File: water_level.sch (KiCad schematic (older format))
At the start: 16 parts

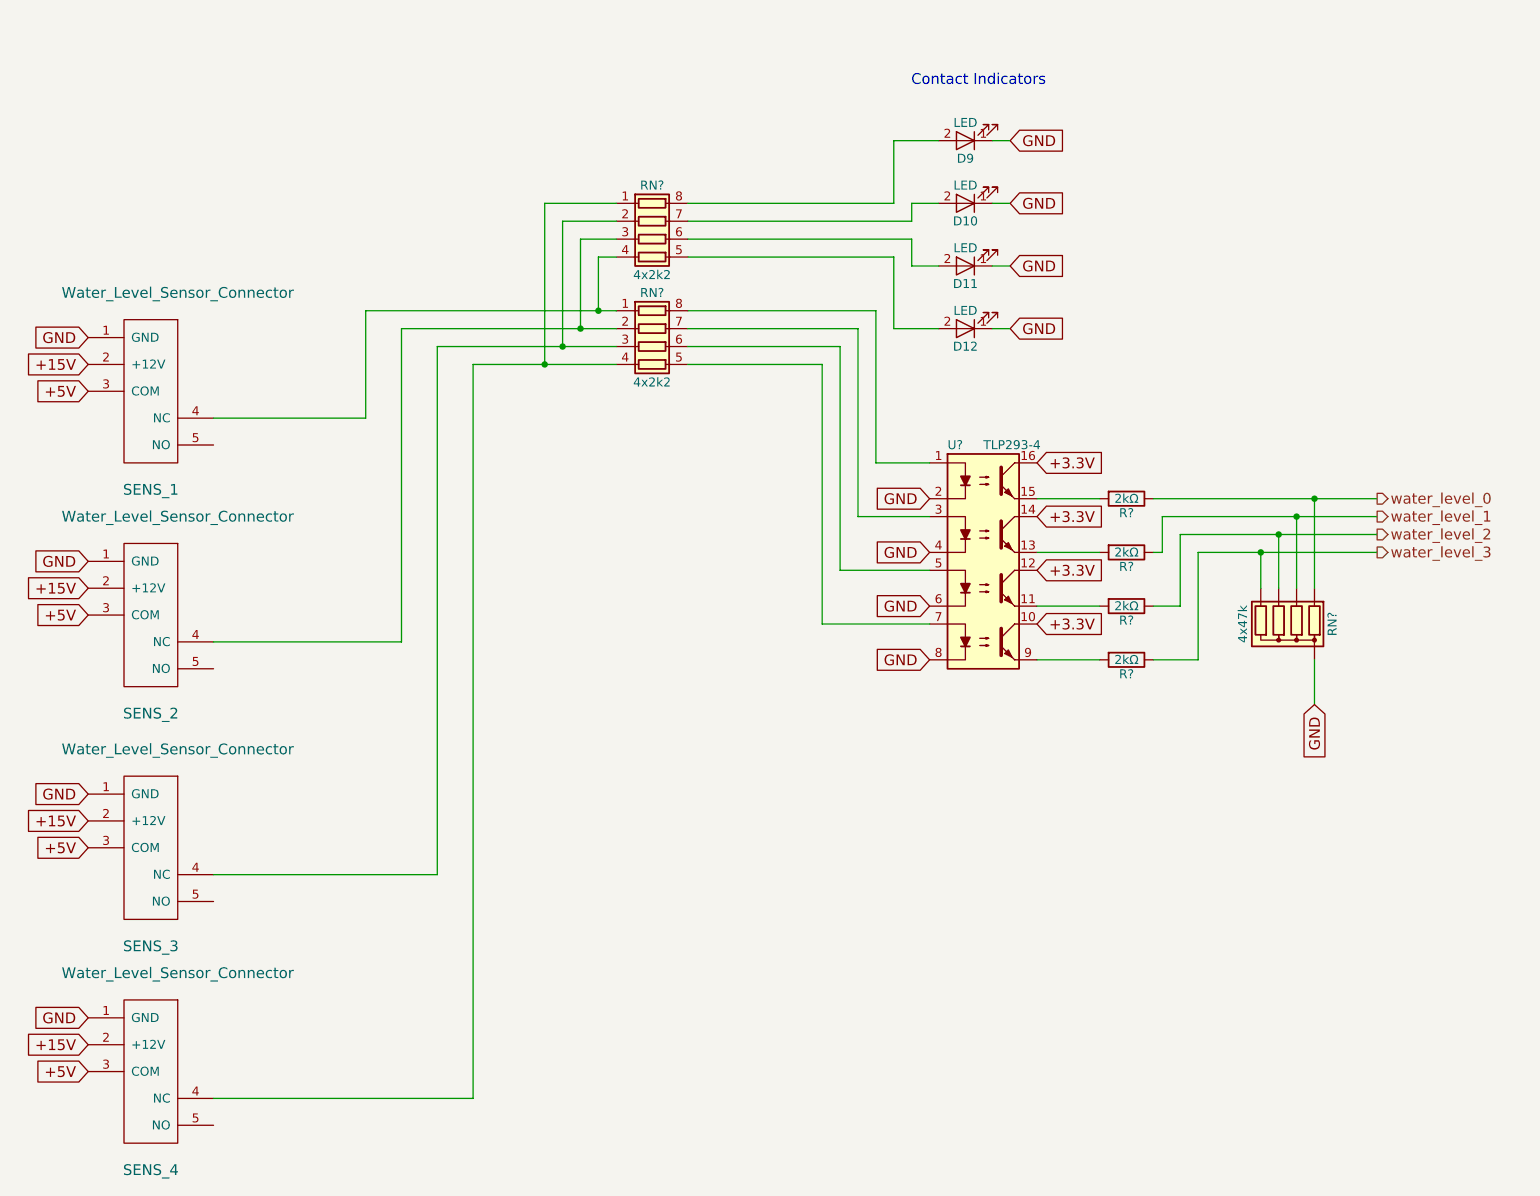
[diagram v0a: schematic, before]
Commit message: some issues fixed by the bugfixer; formal verification needed
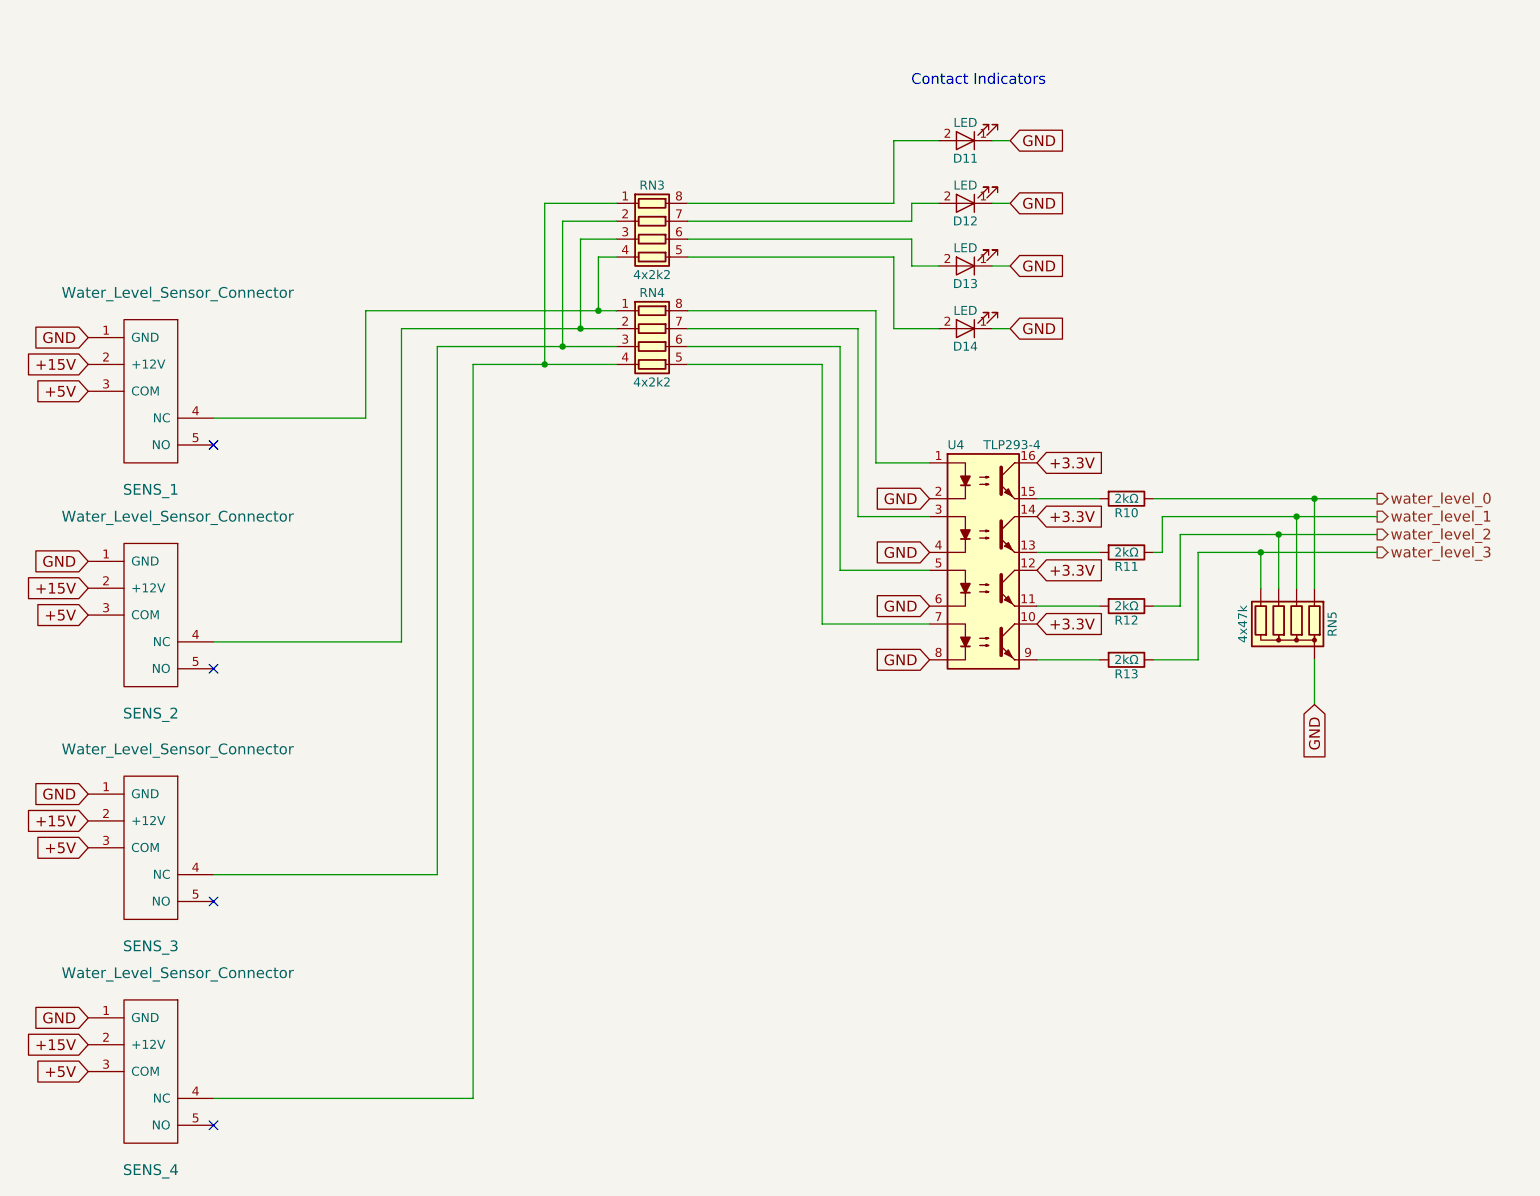
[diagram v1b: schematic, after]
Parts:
- gave numbers to parts that had none: 8
- renumbered D9 to D11, D10 to D12, D11 to D13, D12 to D14
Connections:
- no-connect marks 0 -> 4
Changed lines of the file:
@@
 $EndComp
 $Comp
-L LED D11
+L LED D13
 U 1 1 59403F87
 P 8000 2450
-F 0 "D11" H 8000 2550 50  0000 C CNN
+F 0 "D13" H 8000 2550 50  0000 C CNN
 F 1 "LED" H 8000 2350 50  0000 C CNN
 F 2 "LEDs:LED_1206" H 8000 2450 50  0001 C CNN
@@
 	8250 2450 8150 2450
 $Comp
-L LED D12
+L LED D14
 U 1 1 5940539F
 P 8000 2800
-F 0 "D12" H 8000 2900 50  0000 C CNN
+F 0 "D14" H 8000 2900 50  0000 C CNN
 F 1 "LED" H 8000 2700 50  0000 C CNN
 F 2 "LEDs:LED_1206" H 8000 2800 50  0001 C CNN
@@
 	8250 2800 8150 2800
 $Comp
-L LED D10
+L LED D12
 U 1 1 59405535
 P 8000 2100
-F 0 "D10" H 8000 2200 50  0000 C CNN
+F 0 "D12" H 8000 2200 50  0000 C CNN
 F 1 "LED" H 8000 2000 50  0000 C CNN
 F 2 "LEDs:LED_1206" H 8000 2100 50  0001 C CNN
@@
 	8250 2100 8150 2100
 $Comp
-L LED D9
+L LED D11
 U 1 1 59405613
 P 8000 1750
-F 0 "D9" H 8000 1850 50  0000 C CNN
+F 0 "D11" H 8000 1850 50  0000 C CNN
 F 1 "LED" H 8000 1650 50  0000 C CNN
 F 2 "LEDs:LED_1206" H 8000 1750 50  0001 C CNN
@@
 +5V
 $Comp
-L R_Network04 RN?
+L R_Network04 RN5
 U 1 1 59A52B59
 P 9750 4450
-F 0 "RN?" V 9450 4450 50  0000 C CNN
+F 0 "RN5" V 9450 4450 50  0000 C CNN
 F 1 "4x47k" V 9950 4450 50  0000 C CNN
 F 2 "kilibs:YC164-Yageo-Handsoldering" V 10025 4450 50  0001 C CNN
@@
 Connection ~ 9950 3750
 $Comp
-L LTV-847 U?
+L LTV-847 U4
 U 1 1 59A57625
 P 8100 4150
-F 0 "U?" H 7900 4850 50  0000 L CNN
+F 0 "U4" H 7900 4850 50  0000 L CNN
 F 1 "TLP293-4" H 8100 4850 50  0000 L CNN
 F 2 "Housings_SOIC:SOIC-16_3.9x9.9mm_Pitch1.27mm" H 7900 3550 50  0001 L CIN
@@
 $EndComp
 $Comp
-L R R?
+L R R10
 U 1 1 59A580D3
 P 8900 3750
-F 0 "R?" V 8980 3750 50  0000 C CNN
+F 0 "R10" V 8980 3750 50  0000 C CNN
 F 1 "2kΩ" V 8900 3750 50  0000 C CNN
 F 2 "Resistors_SMD:R_0603_HandSoldering" V 8830 3750 50  0001 C CNN
@@
 	5650 2100 6050 2100
 $Comp
-L R_Pack04 RN?
+L R_Pack04 RN3
 U 1 1 59A818FC
 P 6250 2300
-F 0 "RN?" V 5950 2300 50  0000 C CNN
+F 0 "RN3" V 5950 2300 50  0000 C CNN
 F 1 "4x2k2" V 6450 2300 50  0000 C CNN
 F 2 "kilibs:YC164-Yageo-Handsoldering" V 6525 2300 50  0001 C CNN
@@
 $EndComp
 $Comp
-L R_Pack04 RN?
+L R_Pack04 RN4
 U 1 1 59A81B85
 P 6250 2900
-F 0 "RN?" V 5950 2900 50  0000 C CNN
+F 0 "RN4" V 5950 2900 50  0000 C CNN
 F 1 "4x2k2" V 6450 2900 50  0000 C CNN
 F 2 "kilibs:YC164-Yageo-Handsoldering" V 6525 2900 50  0001 C CNN
@@
 $EndComp
 $Comp
-L R R?
+L R R11
 U 1 1 59A9482F
 P 8900 4050
-F 0 "R?" V 8980 4050 50  0000 C CNN
+F 0 "R11" V 8980 4050 50  0000 C CNN
 F 1 "2kΩ" V 8900 4050 50  0000 C CNN
 F 2 "Resistors_SMD:R_0603_HandSoldering" V 8830 4050 50  0001 C CNN
@@
 $EndComp
 $Comp
-L R R?
+L R R12
 U 1 1 59A94875
 P 8900 4350
-F 0 "R?" V 8980 4350 50  0000 C CNN
+F 0 "R12" V 8980 4350 50  0000 C CNN
 F 1 "2kΩ" V 8900 4350 50  0000 C CNN
 F 2 "Resistors_SMD:R_0603_HandSoldering" V 8830 4350 50  0001 C CNN
@@
 $EndComp
 $Comp
-L R R?
+L R R13
 U 1 1 59A948BA
 P 8900 4650
-F 0 "R?" V 8980 4650 50  0000 C CNN
+F 0 "R13" V 8980 4650 50  0000 C CNN
 F 1 "2kΩ" V 8900 4650 50  0000 C CNN
 F 2 "Resistors_SMD:R_0603_HandSoldering" V 8830 4650 50  0001 C CNN
@@
 	0    1    1    0
 $EndComp
+NoConn ~ 3800 4700
+NoConn ~ 3800 3450
+NoConn ~ 3800 6000
+NoConn ~ 3800 7250
 $EndSCHEMATC

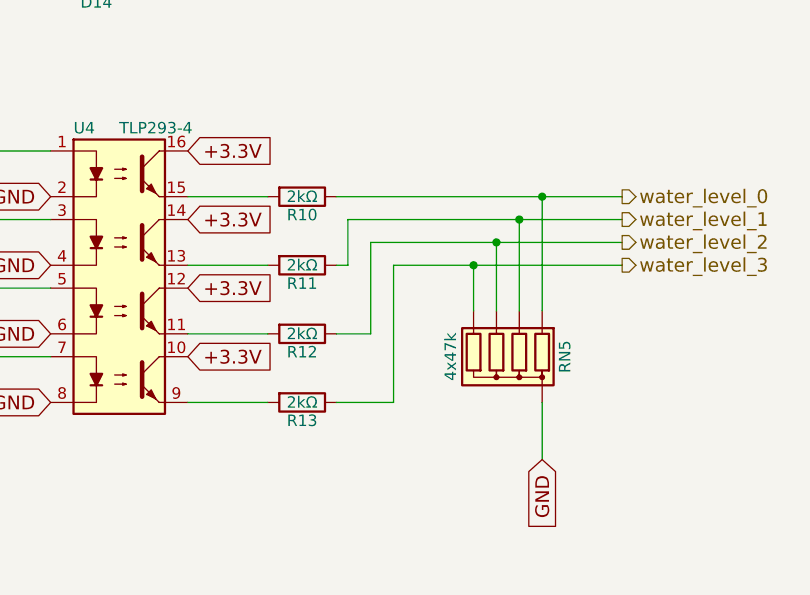
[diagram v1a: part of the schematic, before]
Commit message: I have verified the schematic a second time (except the so-dimm), and I have selected all of the components with links and footprint. I need to verify the schematic a third time and root
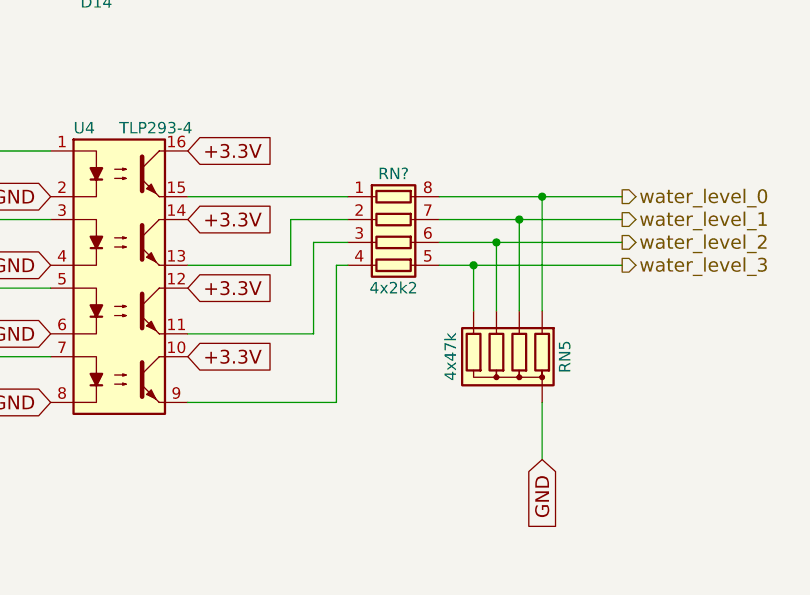
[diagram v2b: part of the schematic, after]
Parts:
- removed R10, R11, R12, R13: 2kΩ, Resistors_SMD:R_0603_HandSoldering, symbol R
- added RN?: 4x2k2, kilibs:YC164-Yageo-Handsoldering, symbol R_Pack04
- RN5: footprint kilibs:YC164-Yageo-Handsoldering -> water:YC158-Yageo-Handsoldering
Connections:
- net water_level_0: now also RN?.8 (R1.2)
- net water_level_1: now also RN?.7 (R2.2)
- net water_level_2: now also RN?.6 (R3.2)
- net water_level_3: now also RN?.5 (R4.2)
- net at U4.11: now also RN?.3 (R3.1)
- net at U4.13: now also RN?.2 (R2.1)
- net at U4.15: now also RN?.1 (R1.1)
- net at U4.9: now also RN?.4 (R4.1)
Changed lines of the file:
@@
 F 0 "RN5" V 9450 4450 50  0000 C CNN
 F 1 "4x47k" V 9950 4450 50  0000 C CNN
-F 2 "kilibs:YC164-Yageo-Handsoldering" V 10025 4450 50  0001 C CNN
+F 2 "water:YC158-Yageo-Handsoldering" V 10025 4450 50  0001 C CNN
 F 3 "http://hu.farnell.com/yageo-phycomp/yc158tjr-0747kl/resistor-network-rna310-1206-47k/dp/9236279" H 9750 4450 50  0001 C CNN
 	1    9750 4450
@@
 Wire Wire Line
 	9950 4900 9950 4650
-Wire Wire Line
-	9050 3750 10300 3750
-Wire Wire Line
-	9100 3850 10300 3850
-Wire Wire Line
-	9200 3950 10300 3950
-Wire Wire Line
-	9300 4050 10300 4050
 Wire Wire Line
 	9650 4250 9650 4050
@@
 	1    0    0    -1
 $EndComp
-$Comp
-L R R10
-U 1 1 59A580D3
-P 8900 3750
-F 0 "R10" V 8980 3750 50  0000 C CNN
-F 1 "2kΩ" V 8900 3750 50  0000 C CNN
-F 2 "Resistors_SMD:R_0603_HandSoldering" V 8830 3750 50  0001 C CNN
-F 3 "hu.farnell.com/multicomp/mcwr06x2001ftl/res-thick-film-2k-1-0-1w-0603/dp/2447319" H 8900 3750 50  0001 C CNN
-	1    8900 3750
-	0    1    1    0
-$EndComp
-Wire Wire Line
-	8750 3750 8400 3750
-Wire Wire Line
-	8400 4050 8750 4050
-Wire Wire Line
-	8400 4350 8750 4350
-Wire Wire Line
-	8400 4650 8750 4650
-Wire Wire Line
-	9100 3850 9100 4050
-Wire Wire Line
-	9100 4050 9050 4050
-Wire Wire Line
-	9200 3950 9200 4350
-Wire Wire Line
-	9200 4350 9050 4350
-Wire Wire Line
-	9300 4050 9300 4650
-Wire Wire Line
-	9300 4650 9050 4650
+Wire Wire Line
+	8400 3750 9100 3750
+Wire Wire Line
+	8400 4050 8850 4050
+Wire Wire Line
+	8400 4350 8950 4350
+Wire Wire Line
+	8400 4650 9050 4650
 Wire Wire Line
 	7500 2700 7500 3550
@@
 	0    1    1    0
 $EndComp
-$Comp
-L R R11
-U 1 1 59A9482F
-P 8900 4050
-F 0 "R11" V 8980 4050 50  0000 C CNN
-F 1 "2kΩ" V 8900 4050 50  0000 C CNN
-F 2 "Resistors_SMD:R_0603_HandSoldering" V 8830 4050 50  0001 C CNN
-F 3 "hu.farnell.com/multicomp/mcwr06x2001ftl/res-thick-film-2k-1-0-1w-0603/dp/2447319" H 8900 4050 50  0001 C CNN
-	1    8900 4050
-	0    1    1    0
-$EndComp
-$Comp
-L R R12
-U 1 1 59A94875
-P 8900 4350
-F 0 "R12" V 8980 4350 50  0000 C CNN
-F 1 "2kΩ" V 8900 4350 50  0000 C CNN
-F 2 "Resistors_SMD:R_0603_HandSoldering" V 8830 4350 50  0001 C CNN
-F 3 "hu.farnell.com/multicomp/mcwr06x2001ftl/res-thick-film-2k-1-0-1w-0603/dp/2447319" H 8900 4350 50  0001 C CNN
-	1    8900 4350
-	0    1    1    0
-$EndComp
-$Comp
-L R R13
-U 1 1 59A948BA
-P 8900 4650
-F 0 "R13" V 8980 4650 50  0000 C CNN
-F 1 "2kΩ" V 8900 4650 50  0000 C CNN
-F 2 "Resistors_SMD:R_0603_HandSoldering" V 8830 4650 50  0001 C CNN
-F 3 "hu.farnell.com/multicomp/mcwr06x2001ftl/res-thick-film-2k-1-0-1w-0603/dp/2447319" H 8900 4650 50  0001 C CNN
-	1    8900 4650
-	0    1    1    0
-$EndComp
 NoConn ~ 3800 4700
 NoConn ~ 3800 3450
 NoConn ~ 3800 6000
 NoConn ~ 3800 7250
+$Comp
+L R_Pack04 RN?
+U 1 1 59A9E3BA
+P 9300 3950
+F 0 "RN?" V 9000 3950 50  0000 C CNN
+F 1 "4x2k2" V 9500 3950 50  0000 C CNN
+F 2 "kilibs:YC164-Yageo-Handsoldering" V 9575 3950 50  0001 C CNN
+F 3 "http://hu.farnell.com/yageo-phycomp/yc164-jr-072k2l/resistor-array-arv241-1206-2k2/dp/9234535" H 9300 3950 50  0001 C CNN
+	1    9300 3950
+	0    1    1    0
+$EndComp
+Wire Wire Line
+	9500 3750 10300 3750
+Wire Wire Line
+	9500 3850 10300 3850
+Wire Wire Line
+	9500 3950 10300 3950
+Wire Wire Line
+	9500 4050 10300 4050
+Wire Wire Line
+	9100 3850 8850 3850
+Wire Wire Line
+	8850 3850 8850 4050
+Wire Wire Line
+	9100 3950 8950 3950
+Wire Wire Line
+	8950 3950 8950 4350
+Wire Wire Line
+	9100 4050 9050 4050
+Wire Wire Line
+	9050 4050 9050 4650
 $EndSCHEMATC

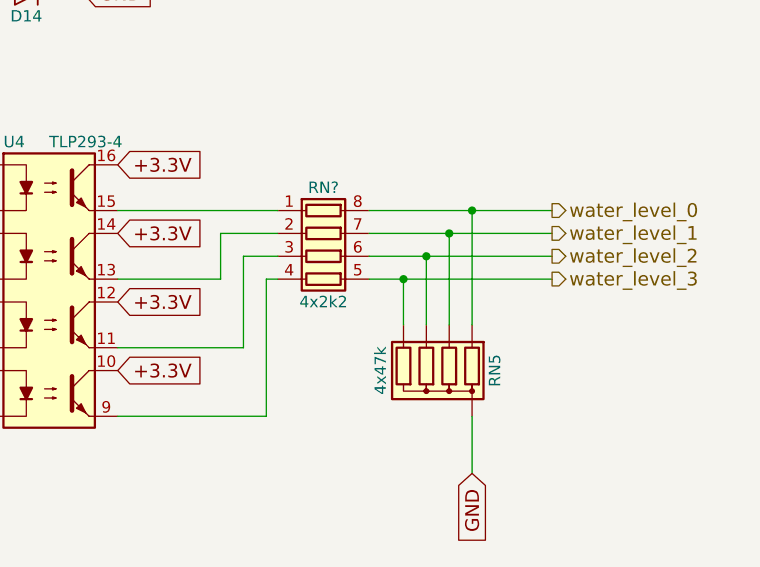
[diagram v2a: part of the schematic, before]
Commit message: part numbers generated;
pcb generation started
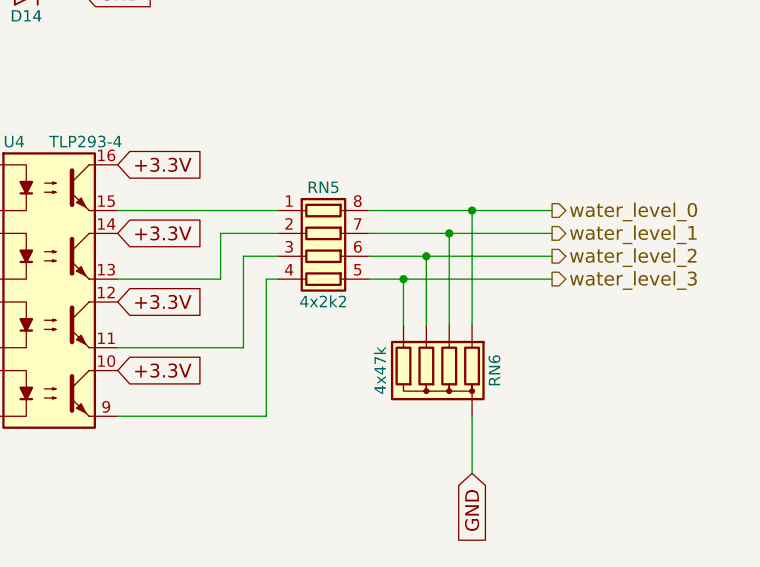
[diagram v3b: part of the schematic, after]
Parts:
- gave numbers to parts that had none: 1
- renumbered RN5 to RN6
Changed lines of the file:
@@
 +5V
 $Comp
-L R_Network04 RN5
+L R_Network04 RN6
 U 1 1 59A52B59
 P 9750 4450
-F 0 "RN5" V 9450 4450 50  0000 C CNN
+F 0 "RN6" V 9450 4450 50  0000 C CNN
 F 1 "4x47k" V 9950 4450 50  0000 C CNN
 F 2 "water:YC158-Yageo-Handsoldering" V 10025 4450 50  0001 C CNN
@@
 NoConn ~ 3800 7250
 $Comp
-L R_Pack04 RN?
+L R_Pack04 RN5
 U 1 1 59A9E3BA
 P 9300 3950
-F 0 "RN?" V 9000 3950 50  0000 C CNN
+F 0 "RN5" V 9000 3950 50  0000 C CNN
 F 1 "4x2k2" V 9500 3950 50  0000 C CNN
 F 2 "kilibs:YC164-Yageo-Handsoldering" V 9575 3950 50  0001 C CNN
